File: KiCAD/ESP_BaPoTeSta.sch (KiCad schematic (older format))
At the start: 21 parts, among them P1 Progr, P2 Battery, P3 Power, P4 Upload, P5 Config, U1 MCP1700-330, U2 ESP-12, U3 DS18B20, U4 DHT22

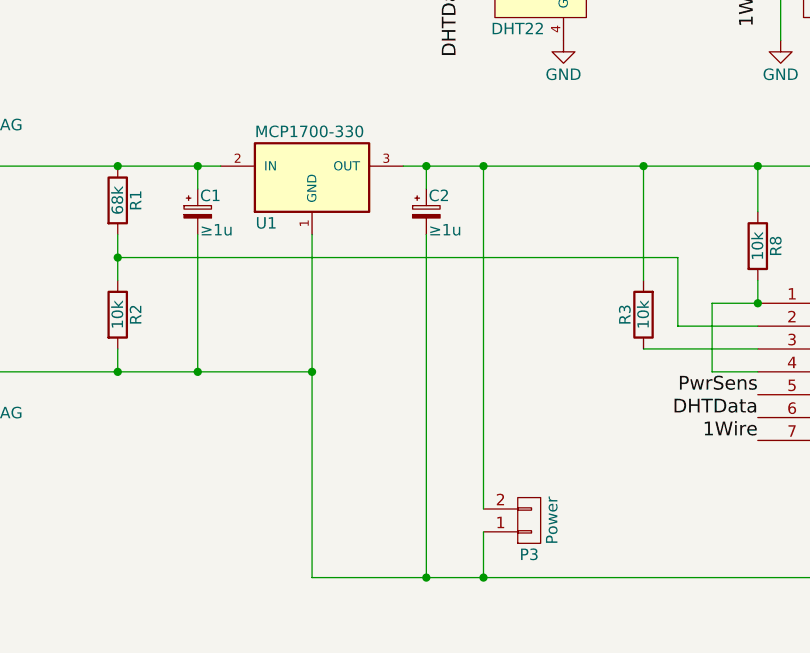
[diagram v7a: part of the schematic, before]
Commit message: ENH: use small ceramic buffer caps
lower ESR. Still use one additional big electrolytic cap
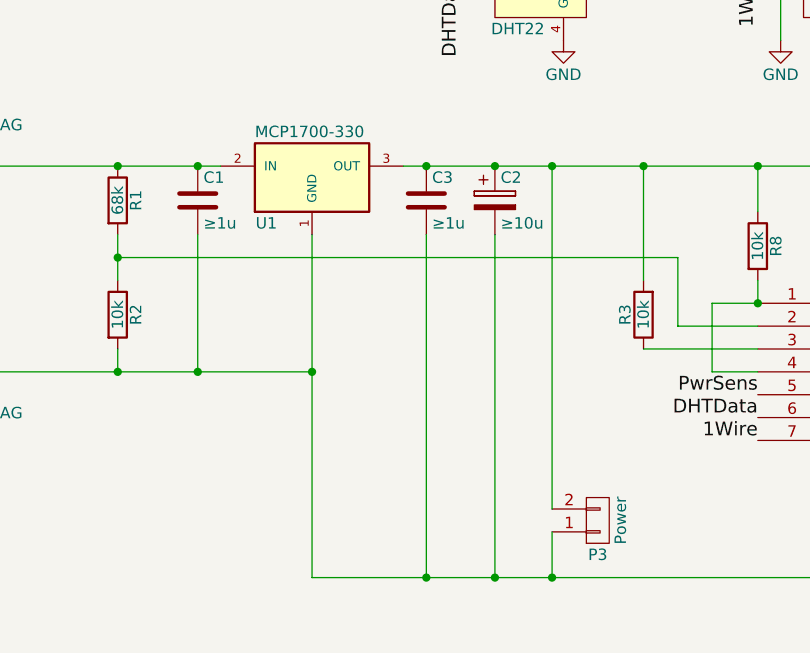
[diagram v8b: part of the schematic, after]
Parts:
- removed C1, C2: ≥1u, Capacitors_ThroughHole:C_Radial_D5_L11_P2, symbol CP_Small
- added C1, C3: ≥1u, Capacitors_SMD:C_1206_HandSoldering, symbol C
- added C2: ≥10u, Capacitors_ThroughHole:C_Radial_D5_L11_P2, symbol CP
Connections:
- net +BATT: now also C1.1
- net GND: now also C1.2, C2.2, C3.2
- net VCC: now also C2.1, C3.1
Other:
- moved on the sheet: P3
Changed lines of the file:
@@
 	-1   0    0    1
 $EndComp
-$Comp
-L CP_Small C1
-U 1 1 5662B5FD
-P 2500 2300
-F 0 "C1" H 2510 2370 50  0000 L CNN
-F 1 "≥1u" H 2510 2220 50  0000 L CNN
-F 2 "Capacitors_ThroughHole:C_Radial_D5_L11_P2" H 2500 2300 50  0001 C CNN
-F 3 "" H 2500 2300 50  0000 C CNN
-	1    2500 2300
-	1    0    0    -1
-$EndComp
-$Comp
-L CP_Small C2
-U 1 1 5662B72E
-P 3500 2300
-F 0 "C2" H 3510 2370 50  0000 L CNN
-F 1 "≥1u" H 3510 2220 50  0000 L CNN
-F 2 "Capacitors_ThroughHole:C_Radial_D5_L11_P2" H 3500 2300 50  0001 C CNN
-F 3 "" H 3500 2300 50  0000 C CNN
-	1    3500 2300
-	1    0    0    -1
-$EndComp
-Wire Wire Line
-	3500 2200 3500 2100
 Connection ~ 3500 2100
 Wire Wire Line
 	3500 2400 3500 3900
 Connection ~ 3500 3900
-Wire Wire Line
-	2500 2200 2500 2100
 Connection ~ 2500 2100
 Wire Wire Line
@@
 L CONN_01X02 P3
 U 1 1 56659295
-P 3950 3650
-F 0 "P3" H 3950 3800 50  0000 C CNN
-F 1 "Power" V 4050 3650 50  0000 C CNN
-F 2 "Pin_Headers:Pin_Header_Straight_1x02" H 3950 3650 50  0001 C CNN
-F 3 "" H 3950 3650 50  0000 C CNN
-	1    3950 3650
-	1    0    0    1
-$EndComp
-Wire Wire Line
-	3750 3900 3750 3700
-Connection ~ 3750 3900
-Wire Wire Line
-	3750 3600 3750 2100
-Connection ~ 3750 2100
+P 4250 3650
+F 0 "P3" H 4250 3800 50  0000 C CNN
+F 1 "Power" V 4350 3650 50  0000 C CNN
+F 2 "Pin_Headers:Pin_Header_Straight_1x02" H 4250 3650 50  0001 C CNN
+F 3 "" H 4250 3650 50  0000 C CNN
+	1    4250 3650
+	1    0    0    1
+$EndComp
+Wire Wire Line
+	4050 3900 4050 3700
+Connection ~ 4050 3900
+Wire Wire Line
+	4050 3600 4050 2100
+Connection ~ 4050 2100
 $Comp
 L R R8
@@
 	4950 2700 4950 2600
 Connection ~ 4950 2700
+$Comp
+L C C1
+U 1 1 56928F2E
+P 2500 2250
+F 0 "C1" H 2525 2350 50  0000 L CNN
+F 1 "≥1u" H 2525 2150 50  0000 L CNN
+F 2 "Capacitors_SMD:C_1206_HandSoldering" H 2538 2100 50  0001 C CNN
+F 3 "" H 2500 2250 50  0000 C CNN
+	1    2500 2250
+	1    0    0    -1
+$EndComp
+$Comp
+L C C3
+U 1 1 5692970C
+P 3500 2250
+F 0 "C3" H 3525 2350 50  0000 L CNN
+F 1 "≥1u" H 3525 2150 50  0000 L CNN
+F 2 "Capacitors_SMD:C_1206_HandSoldering" H 3538 2100 50  0001 C CNN
+F 3 "" H 3500 2250 50  0000 C CNN
+	1    3500 2250
+	1    0    0    -1
+$EndComp
+$Comp
+L CP C2
+U 1 1 56929DFC
+P 3800 2250
+F 0 "C2" H 3825 2350 50  0000 L CNN
+F 1 "≥10u" H 3825 2150 50  0000 L CNN
+F 2 "Capacitors_ThroughHole:C_Radial_D5_L11_P2" H 3838 2100 50  0001 C CNN
+F 3 "" H 3800 2250 50  0000 C CNN
+	1    3800 2250
+	1    0    0    -1
+$EndComp
+Wire Wire Line
+	3800 2400 3800 3900
+Connection ~ 3800 3900
+Connection ~ 3800 2100
 $EndSCHEMATC
